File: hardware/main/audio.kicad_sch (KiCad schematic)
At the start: 0 parts

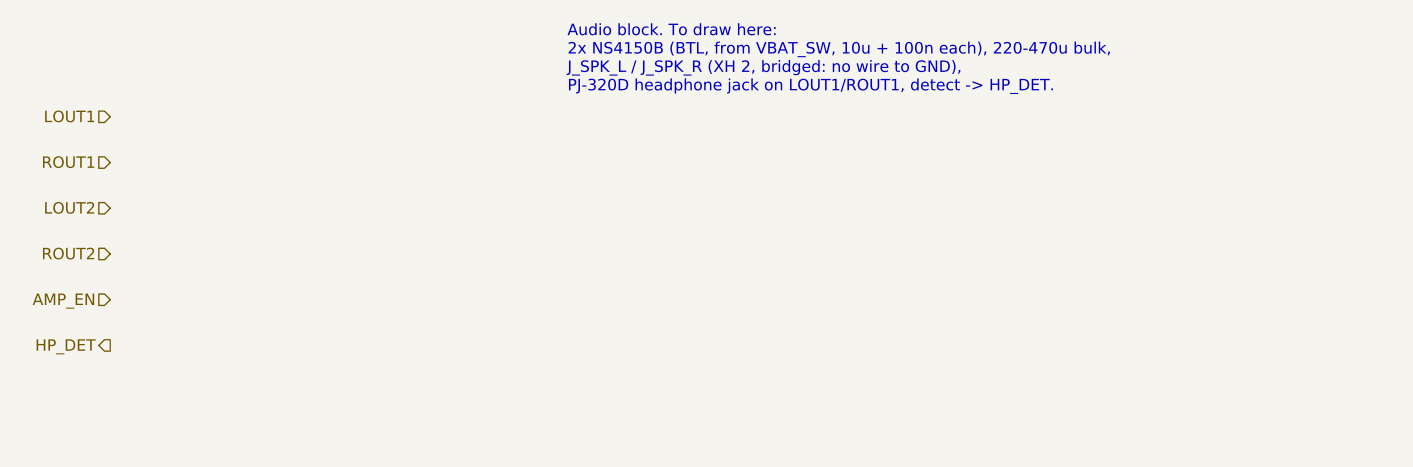
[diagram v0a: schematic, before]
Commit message: hardware: footprints for every part, LCSC library, real A1S pin plan
- lib/lcsc: ESP32-A1S, NS4150B, FS8205A, MSK12C02, PJ-320D imported
  from LCSC with easyeda2kicad (3D paths fixed, NPTH pegs, A1S antenna
  keepout and courtyard), registered in all three projects.
- Parts table with footprint and LCSC number in hardware/README.md.
- The A1S keeps the codec's I2C/I2S inside: display moves to the
  ST7789's pins 14/13/15/22 (SPI or I2C), LED to 12, CHRG/STDBY to 4/2
  through BAT54W. J_SW and J_CHG for an off-board switch and charge LEDs.
- Block sheets use the module's real outputs (HPOUTL/R, SPOLP/N, SPORP/N).

Co-Authored-By: Claude Opus 5.5 <noreply@anthropic.com>
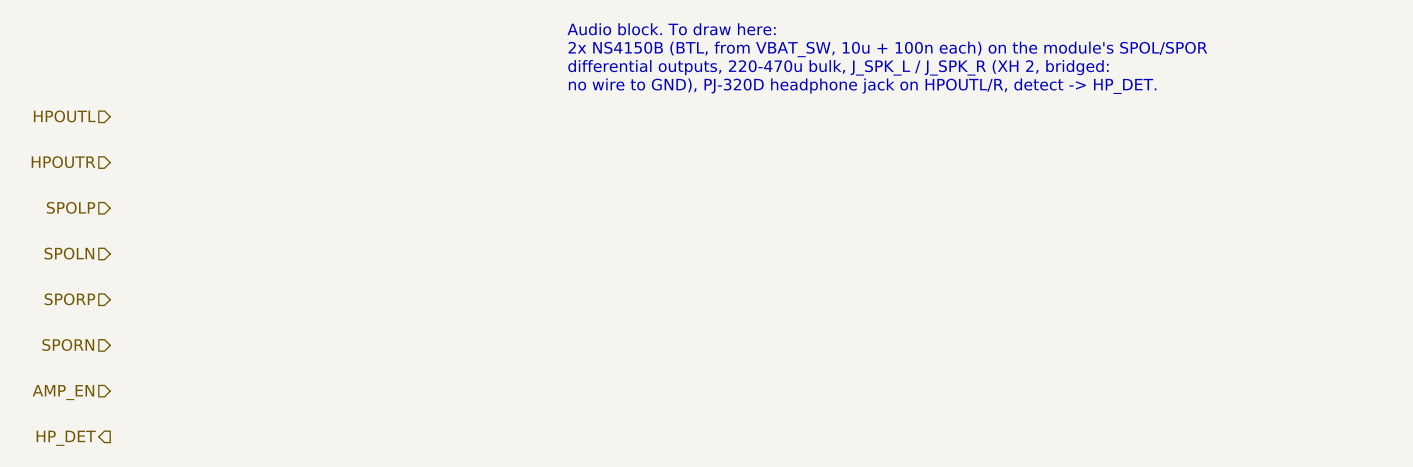
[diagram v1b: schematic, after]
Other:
- note added: "Audio block. To draw here: 2x NS4150B (BTL, from VBAT_SW, 10u + 100n each) on the module's SPOL/SPOR differential outputs, 220-470u bulk, J_SPK_L / J_SPK_R (XH 2, bridged: no wire to GND), PJ-320D headphone jack on HPOUTL/R, detect -> HP_DET."
- note removed: "Audio block. To draw here: 2x NS4150B (BTL, from VBAT_SW, 10u + 100n each), 220-470u bulk, J_SPK_L / J_SPK_R (XH 2, bridged: no wire to GND), PJ-320D headphone jack on LOUT1/ROUT1, detect -> HP_DET."
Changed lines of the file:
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@@
 		(rev "A")
 	)
-	(text "Audio block. To draw here:\n2x NS4150B (BTL, from VBAT_SW, 10u + 100n each), 220-470u bulk,\nJ_SPK_L / J_SPK_R (XH 2, bridged: no wire to GND),\nPJ-320D headphone jack on LOUT1/ROUT1, detect -> HP_DET."
+	(text "Audio block. To draw here:\n2x NS4150B (BTL, from VBAT_SW, 10u + 100n each) on the module's SPOL/SPOR\ndifferential outputs, 220-470u bulk, J_SPK_L / J_SPK_R (XH 2, bridged:\nno wire to GND), PJ-320D headphone jack on HPOUTL/R, detect -> HP_DET."
 		(exclude_from_sim no)
 		(at 101.6 40.64 0)
@@
 		)
 	)
-	(hierarchical_label "LOUT2"
+	(hierarchical_label "HPOUTL"
+		(shape input)
+		(at 50.8 50.8 180)
+		(effects
+			(font
+				(size 1.27 1.27)
+			)
+			(justify right)
+		)
+	)
+	(hierarchical_label "HP_DET"
+		(shape output)
+		(at 50.8 86.36 180)
+		(effects
+			(font
+				(size 1.27 1.27)
+			)
+			(justify right)
+		)
+	)
+	(hierarchical_label "SPORN"
+		(shape input)
+		(at 50.8 76.2 180)
+		(effects
+			(font
+				(size 1.27 1.27)
+			)
+			(justify right)
+		)
+	)
+	(hierarchical_label "HPOUTR"
+		(shape input)
+		(at 50.8 55.88 180)
+		(effects
+			(font
+				(size 1.27 1.27)
+			)
+			(justify right)
+		)
+	)
+	(hierarchical_label "SPOLP"
 		(shape input)
 		(at 50.8 60.96 180)
@@
 	(hierarchical_label "AMP_EN"
 		(shape input)
+		(at 50.8 81.28 180)
+		(effects
+			(font
+				(size 1.27 1.27)
+			)
+			(justify right)
+		)
+	)
+	(hierarchical_label "SPORP"
+		(shape input)
 		(at 50.8 71.12 180)
 		(effects
@@
 		)
 	)
-	(hierarchical_label "ROUT2"
+	(hierarchical_label "SPOLN"
 		(shape input)
 		(at 50.8 66.04 180)
 		(effects
 			(font
-				(size 1.27 1.27)
-			)
-			(justify right)
-		)
-	)
-	(hierarchical_label "HP_DET"
-		(shape output)
-		(at 50.8 76.2 180)
-		(effects
-			(font
-				(size 1.27 1.27)
-			)
-			(justify right)
-		)
-	)
-	(hierarchical_label "ROUT1"
-		(shape input)
-		(at 50.8 55.88 180)
-		(effects
-			(font
-				(size 1.27 1.27)
-			)
-			(justify right)
-		)
-	)
-	(hierarchical_label "LOUT1"
-		(shape input)
-		(at 50.8 50.8 180)
-		(effects
-			(font

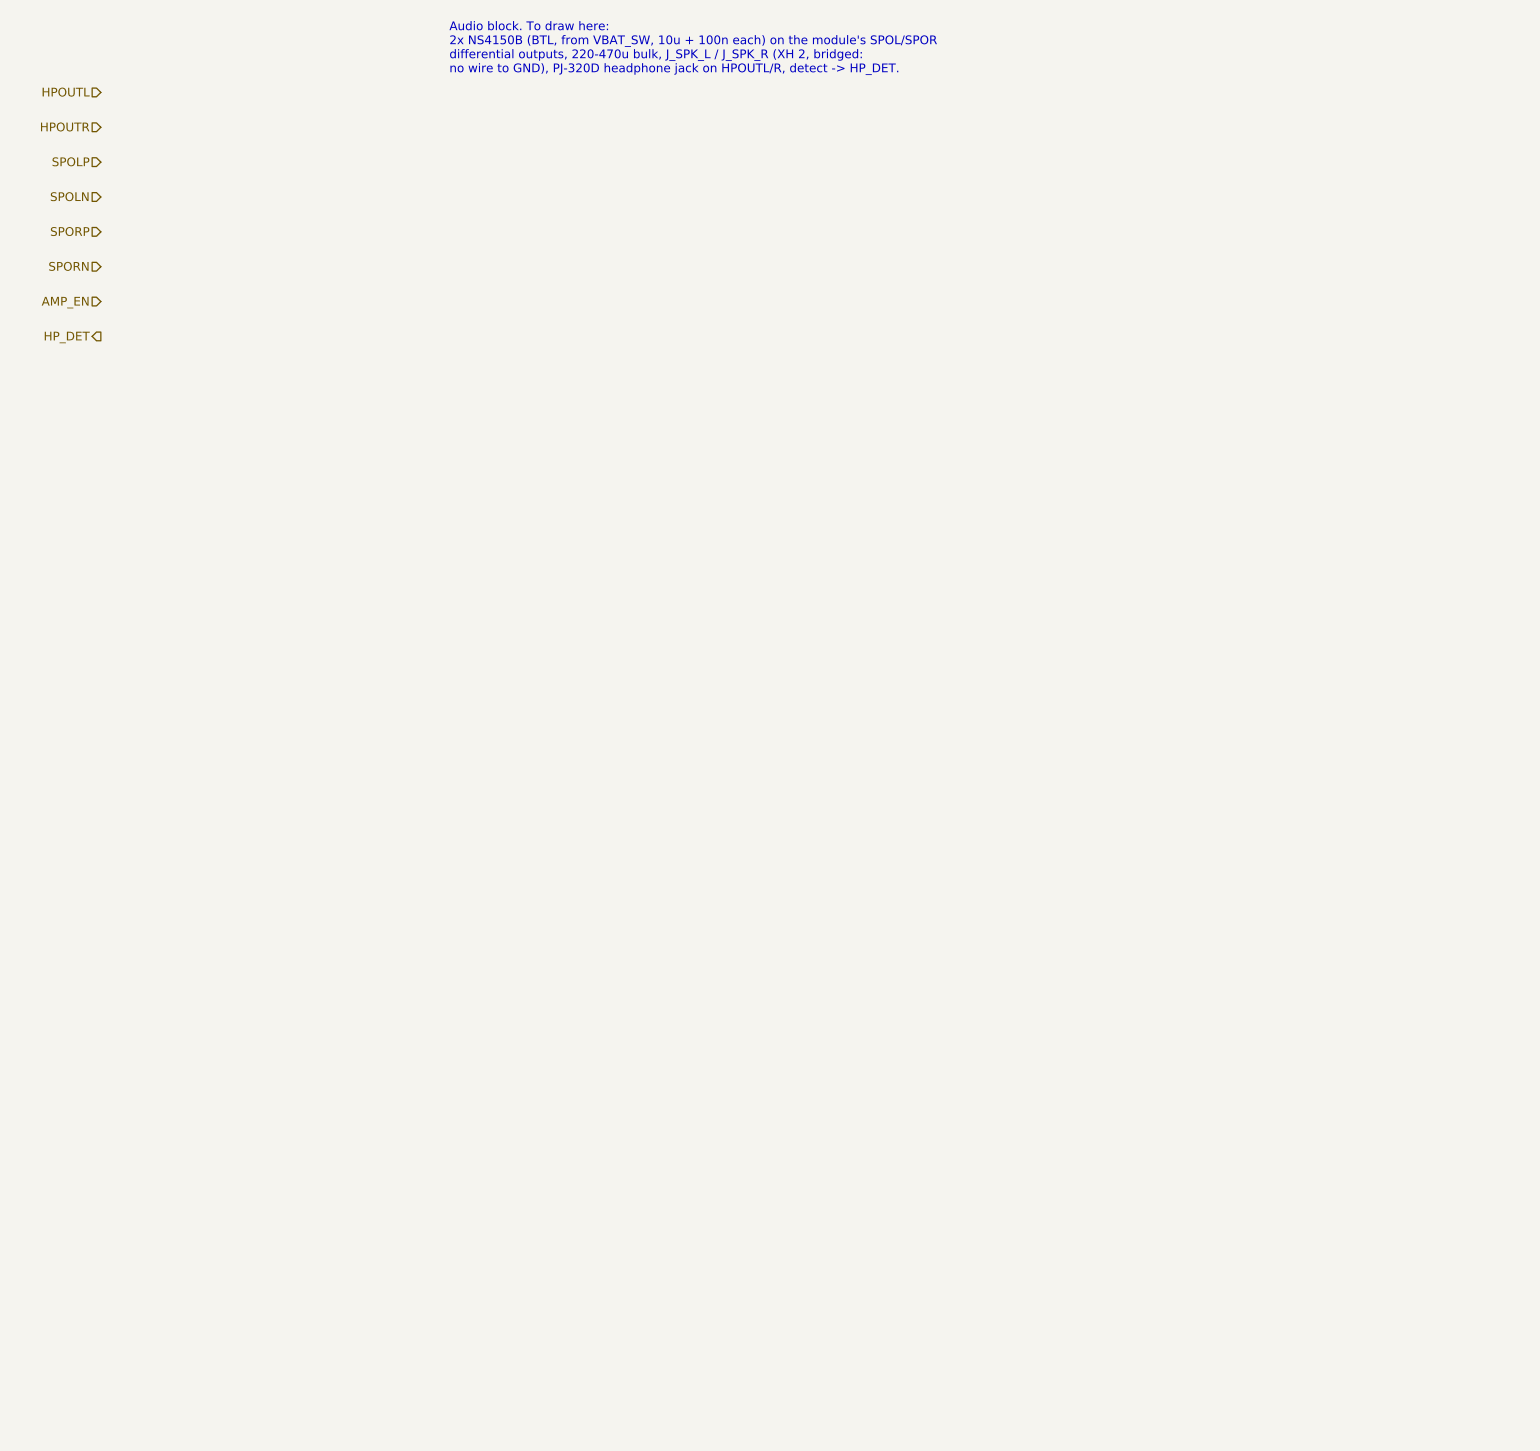
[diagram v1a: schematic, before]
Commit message: hardware: USB, Audio and Connectors sheets; main board ERC clean
Co-Authored-By: Claude Opus 5.5 <noreply@anthropic.com>
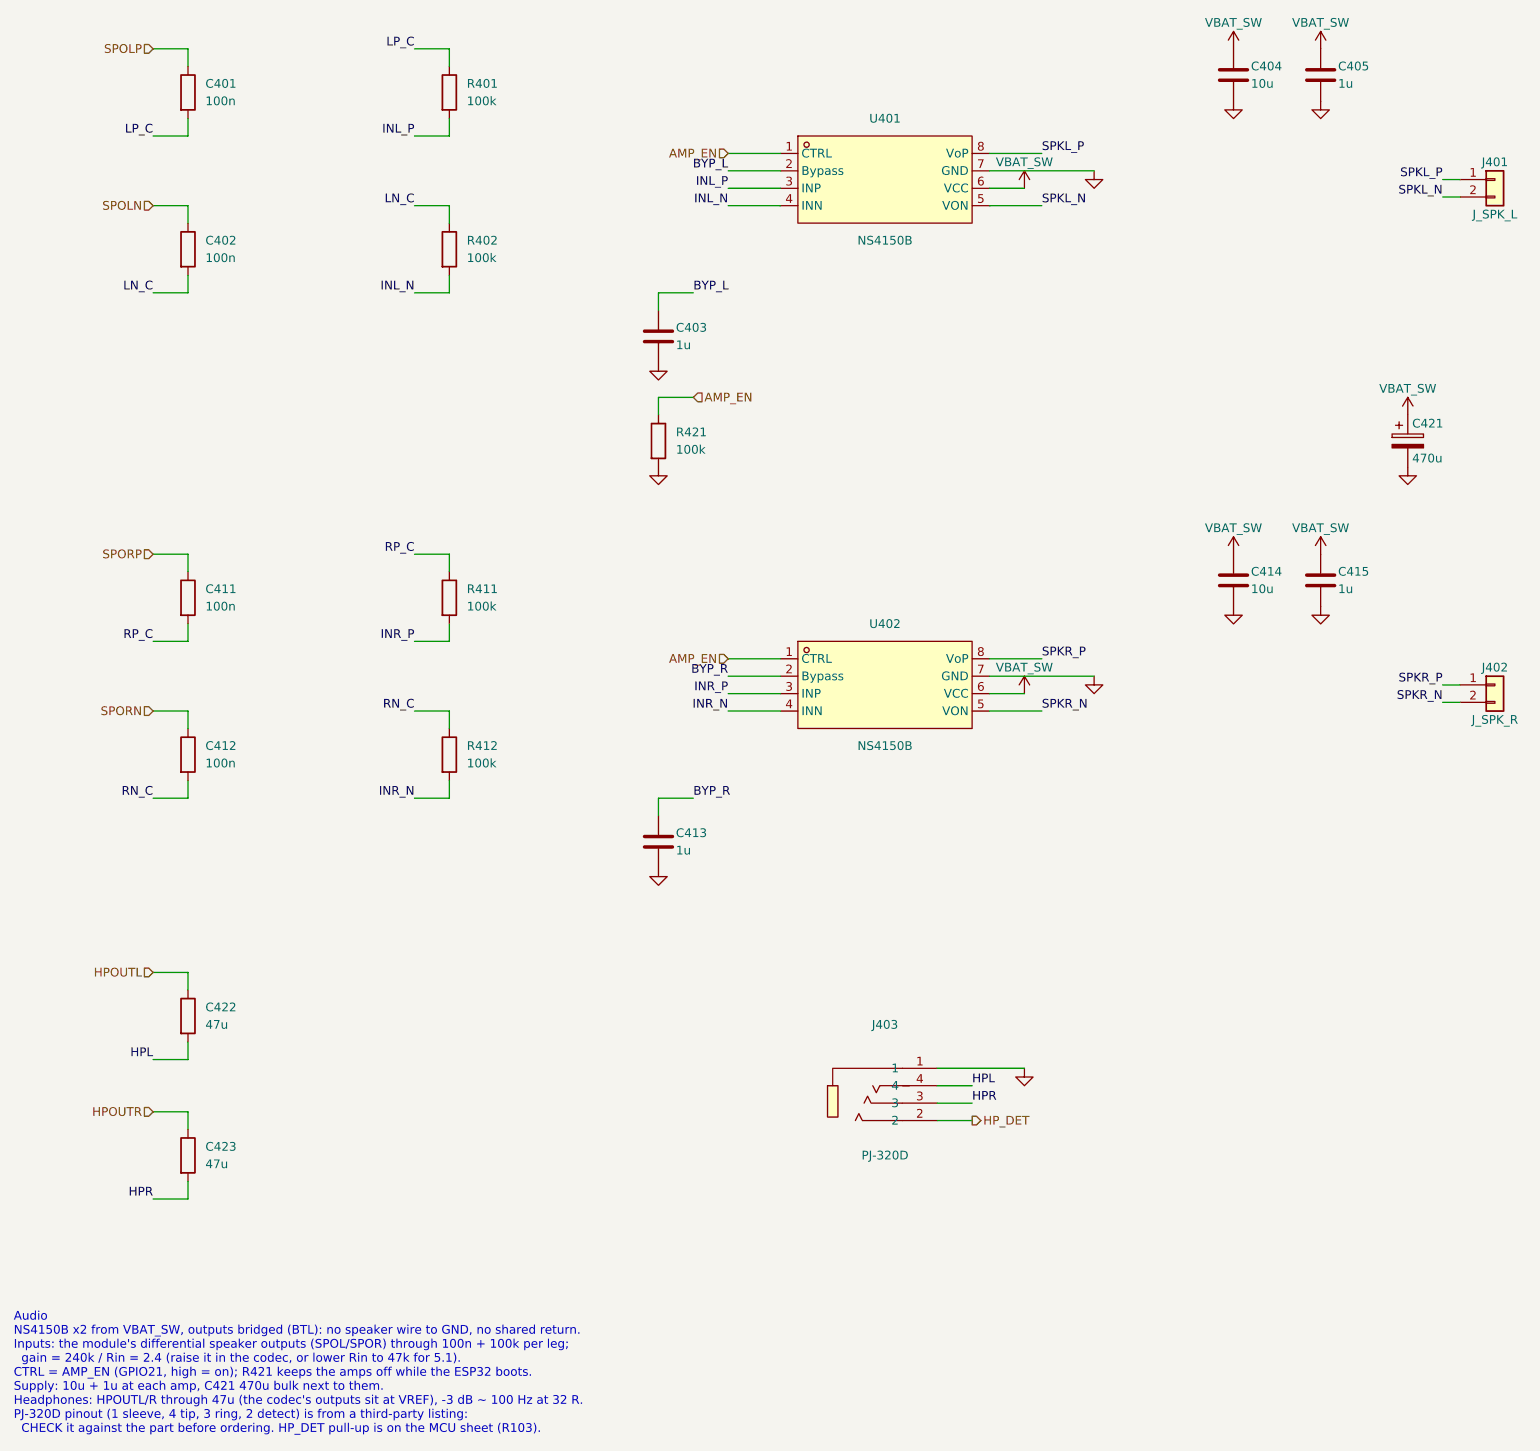
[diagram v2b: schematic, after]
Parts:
- added C401, C402, C411, C412: 100n, Capacitor_SMD:C_0805_2012Metric, symbol Device:R
- added C403, C405, C413, C415: 1u, Capacitor_SMD:C_0805_2012Metric, symbol Device:C
- added C404, C414: 10u, Capacitor_SMD:C_0805_2012Metric, symbol Device:C
- added C421: 470u, Capacitor_SMD:CP_Elec_8x10, symbol Device:C_Polarized
- added C422, C423: 47u, Capacitor_SMD:C_0805_2012Metric, symbol Device:R
- added J401: J_SPK_L, Connector_JST:JST_XH_B2B-XH-A_1x02_P2.50mm_Vertical, symbol Connector_Generic:Conn_01x02
- added J402: J_SPK_R, Connector_JST:JST_XH_B2B-XH-A_1x02_P2.50mm_Vertical, symbol Connector_Generic:Conn_01x02
- added J403: PJ-320D, lcsc:AUDIO-SMD_PJ-320D-1, symbol lcsc:PJ-320D
- added R401, R402, R411, R412, R421: 100k, Resistor_SMD:R_0805_2012Metric, symbol Device:R
- added U401, U402: NS4150B, lcsc:MSOP-8_L3.0-W3.0-P0.65-LS5.0-BL, symbol lcsc:NS4150
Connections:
- net AMP_EN: now also R421.1, U401.1 (CTRL), U402.1 (CTRL)
- net HPOUTL: now also C422.1
- net HPOUTR: now also C423.1
- net HP_DET: now also J403.2
- net SPOLN: now also C402.1
- net SPOLP: now also C401.1
- net SPORN: now also C412.1
- net SPORP: now also C411.1
- new net BYP_L: C403.1, U401.2 (Bypass)
- new net BYP_R: C413.1, U402.2 (Bypass)
- new net GND: C403.2, C404.2, C405.2, C413.2, C414.2, C415.2, C421.2, J403.1, R421.2, U401.7 (GND), U402.7 (GND)
- new net HPL: C422.2, J403.4
- new net HPR: C423.2, J403.3
- new net INL_N: R402.2, U401.4 (INN)
- new net INL_P: R401.2, U401.3 (INP)
- new net INR_N: R412.2, U402.4 (INN)
- new net INR_P: R411.2, U402.3 (INP)
- new net LN_C: C402.2, R402.1
- new net LP_C: C401.2, R401.1
- new net RN_C: C412.2, R412.1
- new net RP_C: C411.2, R411.1
- new net SPKL_N: J401.2 (Pin_2), U401.5 (VON)
- new net SPKL_P: J401.1 (Pin_1), U401.8 (VoP)
- new net SPKR_N: J402.2 (Pin_2), U402.5 (VON)
- new net SPKR_P: J402.1 (Pin_1), U402.8 (VoP)
- new net VBAT_SW: C404.1, C405.1, C414.1, C415.1, C421.1, U401.6 (VCC), U402.6 (VCC)
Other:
- note added: "Audio NS4150B x2 from VBAT_SW, outputs bridged (BTL): no speaker wire to GND, no shared return. Inputs: the module's differential speaker outputs (SPOL/SPOR) through 100n + 100k per leg; gain = 240k / Rin = 2.4 (raise it in the codec, or lower Rin to 47k for 5.1). CTRL = AMP_EN (GPIO21, high = on); R421 keeps the amps off while the ESP32 boots. Supply: 10u + 1u at each amp, C421 470u bulk next to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"
- note removed: "Audio block. To draw here: 2x NS4150B (BTL, from VBAT_SW, 10u + 100n each) on the module's SPOL/SPOR differential outputs, 220-470u bulk, J_SPK_L / J_SPK_R (XH 2, bridged: no wire to GND), PJ-320D headphone jack on HPOUTL/R, detect -> HP_DET."

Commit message: hardware: main board routed and labelled, JLC files
- Freerouting (jar, portable Java 25) via scripts/route.py; net classes
  Power 0.8 mm / Supply 0.4 mm so tracks fit the fine-pitch pins.
- Silkscreen pin names and function labels (silk_main.py), references on
  the fab layer, SMD GND pads solid to the pour; board 100 x 58 mm.
- LCSC numbers on all SMD parts (checked on lcsc.com); jlc.py writes the
  Gerber ZIP, BOM and CPL in JLC's formats.

Co-Authored-By: Claude Opus 5.5 <noreply@anthropic.com>
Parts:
- C401, C402, C411, C412: LCSC (none) -> C49678
- C403, C405, C413, C415: LCSC (none) -> C28323
- C404, C414: LCSC (none) -> C15850
- C421: LCSC (none) -> C249545
- C422, C423: LCSC (none) -> C16780
- R401, R402, R411, R412, R421: LCSC (none) -> C149504
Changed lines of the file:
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@@
+			)
+		)
+		(property "LCSC" "C149504"
+			(at 0 0 0)
+			(hide yes)
+			(effects
+				(font
+					(size 1.27 1.27)
+				)
 			)
 		)
@@
 			)
 		)
+		(property "LCSC" "C149504"
+			(at 0 0 0)
+			(hide yes)
+			(effects
+				(font
+					(size 1.27 1.27)
+				)
+			)
+		)
 		(property "Description" ""
 			(at 101.6 147.32 0)
@@
 			)
 		)
+		(property "LCSC" "C149504"
+			(at 0 0 0)
+			(hide yes)
+			(effects
+				(font
+					(size 1.27 1.27)
+				)
+			)
+		)
 		(property "Description" ""
 			(at 101.6 124.46 0)
@@
 			)
 		)
+		(property "LCSC" "C249545"
+			(at 0 0 0)
+			(hide yes)
+			(effects
+				(font
+					(size 1.27 1.27)
+				)
+			)
+		)
 		(property "Description" ""
 			(at 241.3 101.6 0)
@@
 			)
 		)
+		(property "LCSC" "C49678"
+			(at 0 0 0)
+			(hide yes)
+			(effects
+				(font
+					(size 1.27 1.27)
+				)
+			)
+		)
 		(property "Description" ""
 			(at 63.5 124.46 0)
@@
 			)
 		)
+		(property "LCSC" "C149504"
+			(at 0 0 0)
+			(hide yes)
+			(effects
+				(font
+					(size 1.27 1.27)
+				)
+			)
+		)
 		(property "Description" ""
 			(at 101.6 73.66 0)
@@
 			)
 		)
+		(property "LCSC" "C149504"
+			(at 0 0 0)
+			(hide yes)
+			(effects
+				(font
+					(size 1.27 1.27)
+				)
+			)
+		)
 		(property "Description" ""
 			(at 132.08 101.6 0)
@@
 			)
 		)
+		(property "LCSC" "C28323"
+			(at 0 0 0)
+			(hide yes)
+			(effects
+				(font
+					(size 1.27 1.27)
+				)
+			)
+		)
 		(property "Description" ""
 			(at 132.08 160.02 0)
@@
 			)
 		)
+		(property "LCSC" "C15850"
+			(at 0 0 0)
+			(hide yes)
+			(effects
+				(font
+					(size 1.27 1.27)
+				)
+			)
+		)
 		(property "Description" ""
 			(at 215.9 121.92 0)
@@
 			)
 		)
+		(property "LCSC" "C28323"
+			(at 0 0 0)
+			(hide yes)
+			(effects
+				(font
+					(size 1.27 1.27)
+				)
+			)
+		)
 		(property "Description" ""
 			(at 132.08 86.36 0)
@@
 			)
 		)
+		(property "LCSC" "C16780"
+			(at 0 0 0)
+			(hide yes)
+			(effects
+				(font
+					(size 1.27 1.27)
+				)
+			)
+		)
 		(property "Description" ""
 			(at 63.5 205.74 0)
@@
 			)
 		)
+		(property "LCSC" "C49678"
+			(at 0 0 0)
+			(hide yes)
+			(effects
+				(font
+					(size 1.27 1.27)
+				)
+			)
+		)
 		(property "Description" ""
 			(at 63.5 73.66 0)
@@
 			)
 		)
+		(property "LCSC" "C49678"
+			(at 0 0 0)
+			(hide yes)
+			(effects
+				(font
+					(size 1.27 1.27)
+				)
+			)
+		)
 		(property "Description" ""
 			(at 63.5 147.32 0)
@@
 			)
 		)
+		(property "LCSC" "C28323"
+			(at 0 0 0)
+			(hide yes)
+			(effects
+				(font
+					(size 1.27 1.27)
+				)
+			)
+		)
 		(property "Description" ""
 			(at 228.6 121.92 0)
@@
 			)
 		)
+		(property "LCSC" "C15850"
+			(at 0 0 0)
+			(hide yes)
+			(effects
+				(font
+					(size 1.27 1.27)
+				)
+			)
+		)
 		(property "Description" ""
 			(at 215.9 48.26 0)
@@
 			)
 		)
+		(property "LCSC" "C49678"
+			(at 0 0 0)
+			(hide yes)
+			(effects
+				(font
+					(size 1.27 1.27)
+				)
+			)
+		)
 		(property "Description" ""
 			(at 63.5 50.8 0)
@@
 			)
 		)
+		(property "LCSC" "C28323"
+			(at 0 0 0)
+			(hide yes)
+			(effects
+				(font
+					(size 1.27 1.27)
+				)
+			)
+		)
 		(property "Description" ""
 			(at 228.6 48.26 0)
@@
 			(effects
 				(font
+					(size 1.27 1.27)
+				)
+			)
+		)
+		(property "LCSC" "C16780"
+			(at 0 0 0)
+			(hide yes)
+			(effects
+				(font
